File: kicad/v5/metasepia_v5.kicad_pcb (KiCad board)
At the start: 2 copper layers, 240.6 x 131.9 mm, 74 parts, among them J1 slider

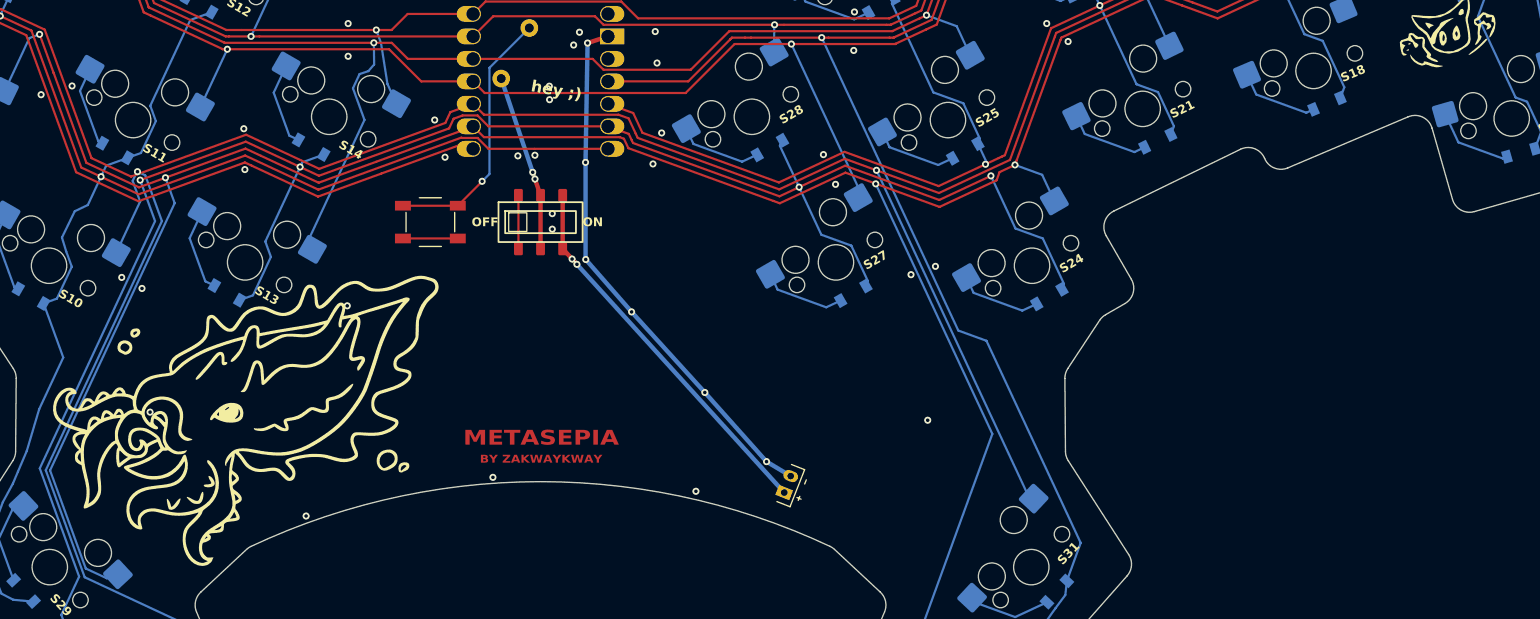
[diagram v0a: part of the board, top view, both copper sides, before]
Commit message: work on plate and change pcb accordingly
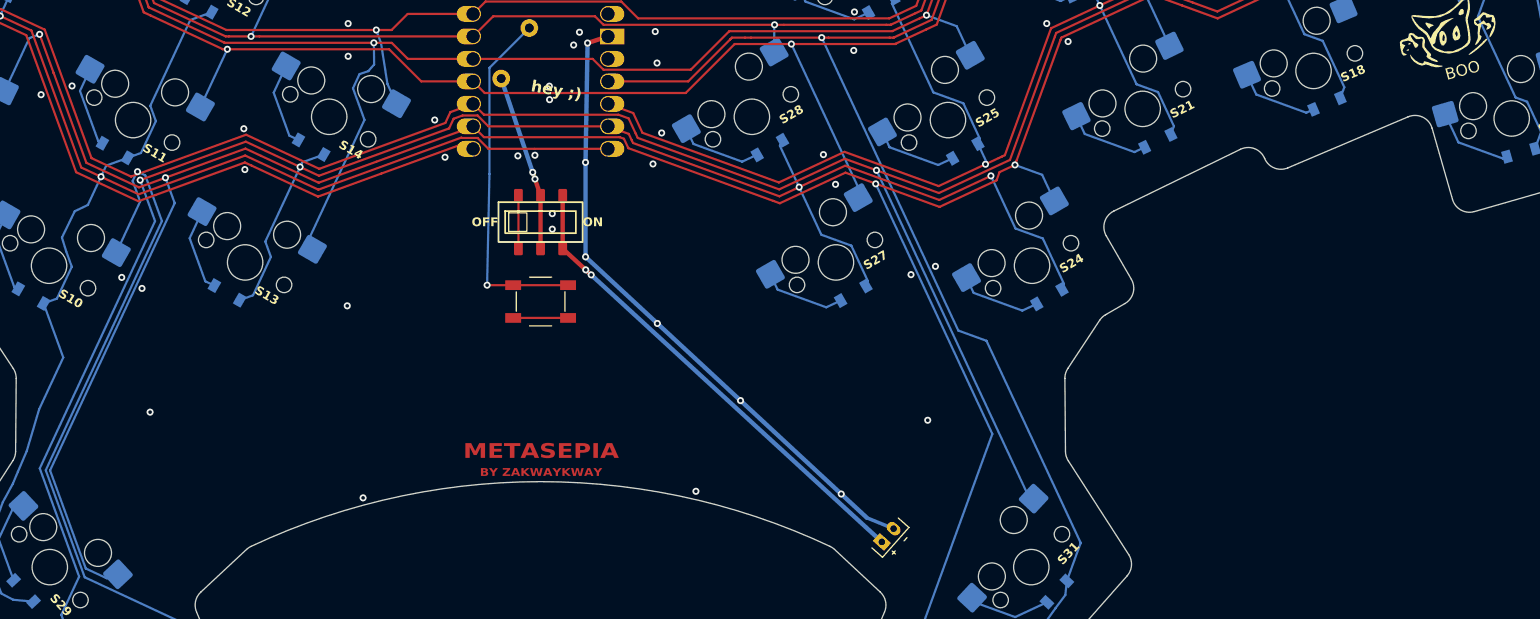
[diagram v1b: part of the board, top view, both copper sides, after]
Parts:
- removed the G*** at (192.7, 157.2)
- moved B1 15.4 mm to (223.6, 143.9)
- moved JST1 12.7 mm to (262.8, 170.3), turned to 48.5 degrees
- moved REF** 1.50 mm to (223.6, 160.8)
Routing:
- net GND: track 66.9 -> 79.4 mm, vias 54 -> 53
- net slider: track 44.0 -> 55.8 mm
- net RST: track 29.6 -> 40.1 mm
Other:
- board text added: "BOO"
